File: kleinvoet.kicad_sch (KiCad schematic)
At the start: 36 parts, among them SW101 RESET, SW102 USER, U101 STM32F446RETx, Y101 12 MHz, Y102 32.768 kHz

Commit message: (pcb) route VCC to audio conn.
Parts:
- added C107: 10u, Capacitor_SMD:C_0402_1005Metric, symbol Device:C_Small
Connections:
- net +3V3: now also C107.1
- net GND: now also C107.2
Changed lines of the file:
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@@
   (junction (at 217.805 56.515) (diameter 0) (color 0 0 0 0)
   )
+  (junction (at 222.885 56.515) (diameter 0) (color 0 0 0 0)
+  )
   (junction (at 123.19 30.48) (diameter 0) (color 0 0 0 0)
   )
@@
   )
   (junction (at 205.74 90.805) (diameter 0) (color 0 0 0 0)
+  )
+  (junction (at 222.885 51.435) (diameter 0) (color 0 0 0 0)
   )
   (junction (at 213.36 80.645) (diameter 0) (color 0 0 0 0)
@@
     (stroke (width 0) (type default))
   )
+  (wire (pts (xy 222.885 51.435) (xy 228.6 51.435))
+    (stroke (width 0) (type default))
+  )
   (wire (pts (xy 115.57 31.75) (xy 115.57 30.48))
     (stroke (width 0) (type default))
@@
   )
   (wire (pts (xy 138.43 102.87) (xy 146.685 102.87))
+    (stroke (width 0) (type default))
+  )
+  (wire (pts (xy 222.885 56.515) (xy 228.6 56.515))
     (stroke (width 0) (type default))
   )
@@
         )
       )
+    )
+  )
+  (symbol (lib_id "Device:C_Small") (at 228.6 53.975 0) (unit 1)
+    (in_bom yes) (on_board yes) (dnp no)
+    (property "Reference" "C107" (at 228.6 46.99 90)
+      (effects (font (size 1.27 1.27)) (justify left))
+    )
+    (property "Value" "10u" (at 227.33 48.895 0)
+      (effects (font (size 1.27 1.27)) (justify left))
+    )
+    (property "Footprint" "Capacitor_SMD:C_0402_1005Metric" (at 228.6 53.975 0)
+      (effects (font (size 1.27 1.27)) hide)
+    )
+    (property "Datasheet" "~" (at 228.6 53.975 0)
+      (effects (font (size 1.27 1.27)) hide)
+    )
+    (property "Notes" "Low ESR" (at 228.6 53.975 0)
+      (effects (font (size 1.27 1.27)) hide)
+    )
+    (property "MPN" "GRM155R60J106ME05D" (at 228.6 53.975 0)
+      (effects (font (size 1.27 1.27)) hide)
+    )
+    (property "Mfr." "Murata" (at 228.6 53.975 0)
+      (effects (font (size 1.27 1.27)) hide)
+    )
+    (pin "1")
+    (pin "2")
+    (instances
+      (project "kleinvoet"
+        (path "/4185c36c-c66e-4dbd-be5d-841e551f4885"
+          (reference "C107") (unit 1)
+        )
+      )

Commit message: (sch) run DRC
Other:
- sheet GNSS_Module ports: added none; removed GPS_INT
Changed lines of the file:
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@@
-    (stroke (width 0) (type default))
-  )
-  (wire (pts (xy 26.67 36.83) (xy 31.75 36.83))
     (stroke (width 0) (type default))
   )
@@
   (label "I2C1_SDA" (at 151.13 97.79 0) (fields_autoplaced)
     (effects (font (size 1.27 1.27)) (justify left bottom))
-  )
-  (label "ADC_SAI_FS" (at 26.67 36.83 180) (fields_autoplaced)
-    (effects (font (size 1.27 1.27)) (justify right bottom))
   )
   (label "I_CHARGE" (at 151.13 80.01 0) (fields_autoplaced)
@@
       (effects (font (size 1.27 1.27)) (justify right))
     )
-    (pin "GPS_INT" input (at 31.75 36.83 180)
-      (effects (font (size 1.27 1.27)) (justify left))
-    )
-    (instances
+    (instances

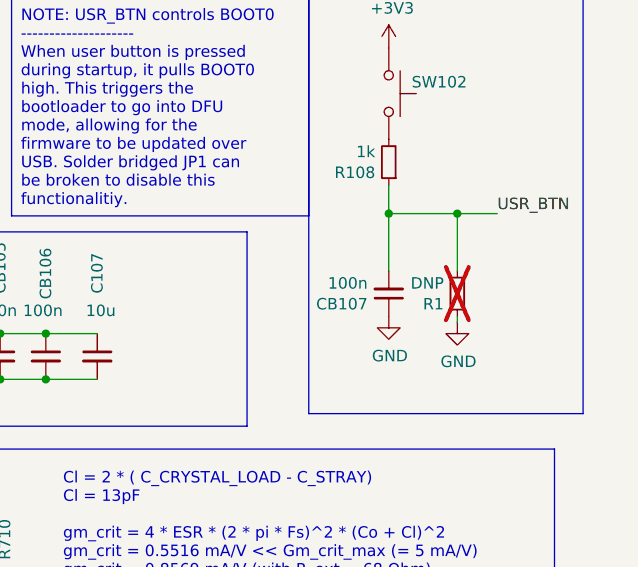
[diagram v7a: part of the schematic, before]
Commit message: (sch) consoldate BOM
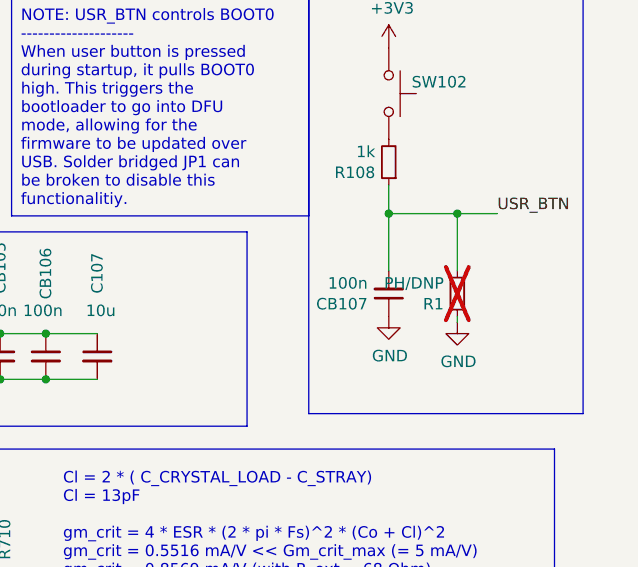
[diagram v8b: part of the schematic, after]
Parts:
- D105: MPN (none) -> SK6805-2427; Mfr. (none) -> Adafruit
- R1: value DNP -> PH/DNP
- R108: MPN (none) -> RT0402FRE071KL
- R904: MPN (none) -> RT0402FRE1310KL
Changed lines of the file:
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@@
       (effects (font (size 1.27 1.27)) (justify left))
     )
-    (property "Value" "DNP" (at 267.1064 45.847 0)
+    (property "Value" "PH/DNP" (at 267.1064 45.847 0)
       (effects (font (size 1.27 1.27)) (justify left))
     )
@@
       (effects (font (size 1.27 1.27)) hide)
     )
-    (property "MPN" "" (at 260.985 32.385 0)
+    (property "MPN" "RT0402FRE071KL" (at 260.985 32.385 0)
       (effects (font (size 1.27 1.27)) hide)
     )
@@
       (effects (font (size 1.27 1.27)) hide)
     )
-    (property "MPN" "" (at 82.55 46.99 0)
+    (property "MPN" "RT0402FRE1310KL" (at 82.55 46.99 0)
       (effects (font (size 1.27 1.27)) hide)
     )
@@
       (effects (font (size 1.27 1.27)) (justify left top) hide)
     )
-    (property "MPN" "" (at 205.74 150.495 0)
-      (effects (font (size 1.27 1.27)) hide)
-    )
-    (property "Mfr." "" (at 205.74 150.495 0)
-      (effects (font (size 1.27 1.27)) hide)
-    )
+    (property "MPN" "SK6805-2427" (at 205.74 150.495 0)
+      (effects (font (size 1.27 1.27)) hide)
+    )
+    (property "Mfr." "Adafruit" (at 205.74 150.495 0)
+      (effects (font (size 1.27 1.27)) hide)
+    )
